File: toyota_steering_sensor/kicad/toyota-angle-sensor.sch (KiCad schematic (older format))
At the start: 30 parts, among them J1 AVR-ISP-6, J2 RJ45, U3 LS7366R, U5 AS5047P, U6 TJA1050, Y1 16MHz

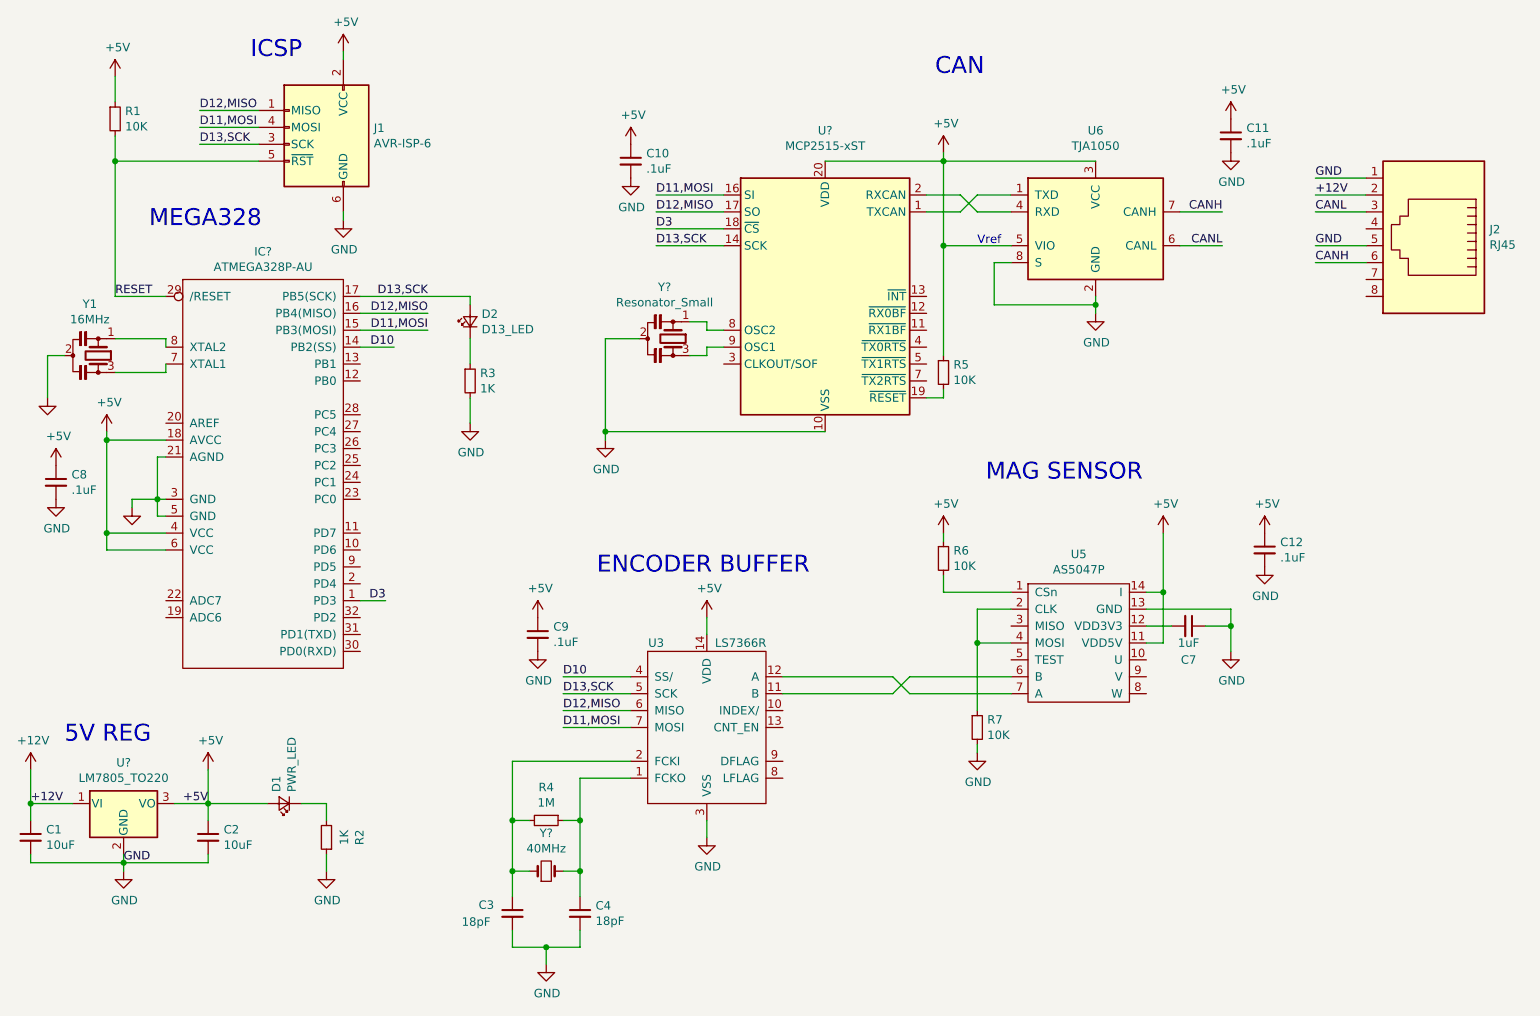
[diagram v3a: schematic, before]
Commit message: modified sch according to V2Changes.txt
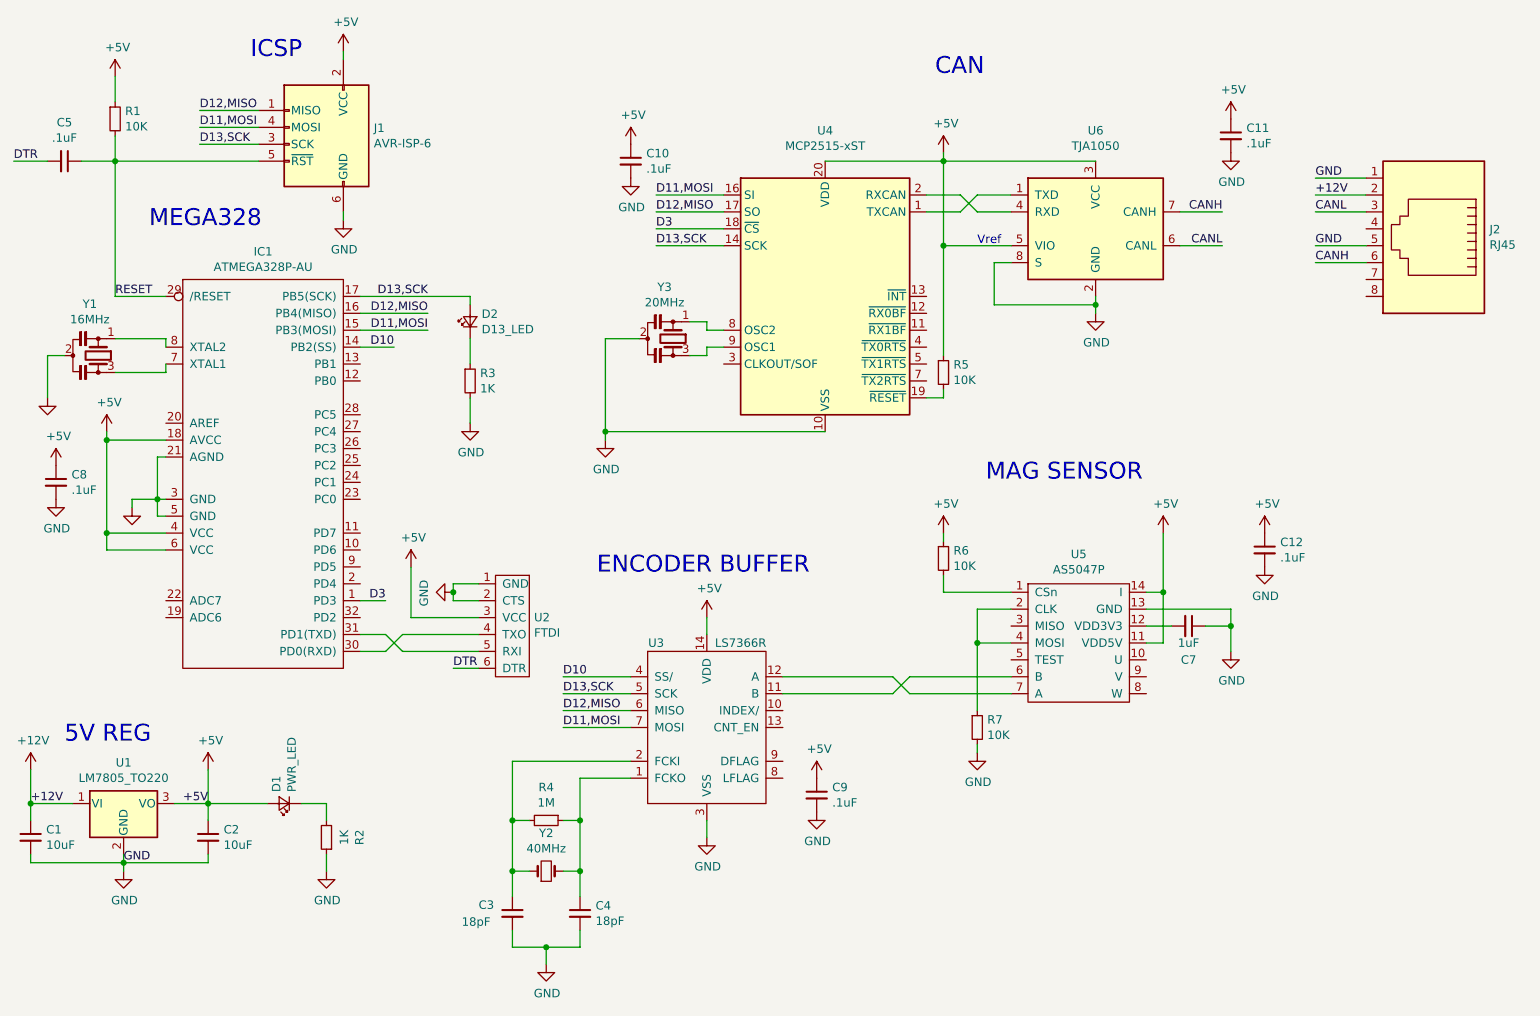
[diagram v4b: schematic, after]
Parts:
- added C5: .1uF, Capacitor_SMD:C_0603_1608Metric, symbol Device:C_Small
- added U2: FTDI, Connector_PinHeader_2.54mm:PinHeader_1x06_P2.54mm_Vertical_SMD_Pin1Left, symbol Angle_Sensor:FTDI
- IC1: renamed from IC?; footprint (none) -> Package_QFP:TQFP-32_7x7mm_P0.8mm
- Y1: footprint Crystal:Resonator_SMD_muRata_CSTxExxV-3Pin_3.0x1.1mm_HandSoldering -> Crystal:Resonator_SMD_muRata_CSTxExxV-3Pin_3.0x1.1mm
- Y3: renamed from Y?; value Resonator_Small -> 20MHz; footprint (none) -> Crystal:Resonator_SMD_muRata_CSTxExxV-3Pin_3.0x1.1mm
- gave numbers to parts that had none: 3
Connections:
- net +5V: now also U2.3 (VCC)
- net GND: now also U2.1 (GND), U2.2 (CTS)
- net RESET: now also C5.1
- net at IC1.30 (PD0(RXD)): now also U2.4 (TXO)
- net at IC1.31 (PD1(TXD)): now also U2.5 (RXI)
- new net DTR: C5.2, U2.6 (DTR)
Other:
- moved on the sheet: C9
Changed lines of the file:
@@
 F 0 "Y1" V 1095 2450 50  0000 C CNN
 F 1 "16MHz" V 1186 2450 50  0000 C CNN
-F 2 "Crystal:Resonator_SMD_muRata_CSTxExxV-3Pin_3.0x1.1mm_HandSoldering" H 1375 2500 50  0001 C CNN
+F 2 "Crystal:Resonator_SMD_muRata_CSTxExxV-3Pin_3.0x1.1mm" H 1375 2500 50  0001 C CNN
 F 3 "~" H 1375 2500 50  0001 C CNN
 F 4 "490-17948-1-ND" H 1400 2500 50  0001 C CNN "Digi-Key Part Number"
@@
 L power:+5V #PWR0103
 U 1 1 5D56B9CD
-P 4000 4050
-F 0 "#PWR0103" H 4000 3900 50  0001 C CNN
-F 1 "+5V" H 4015 4223 50  0000 C CNN
-F 2 "" H 4000 4050 50  0001 C CNN
-F 3 "" H 4000 4050 50  0001 C CNN
-	1    4000 4050
+P 5650 5000
+F 0 "#PWR0103" H 5650 4850 50  0001 C CNN
+F 1 "+5V" H 5665 5173 50  0000 C CNN
+F 2 "" H 5650 5000 50  0001 C CNN
+F 3 "" H 5650 5000 50  0001 C CNN
+	1    5650 5000
 	1    0    0    -1
 $EndComp
@@
 L power:GND #PWR0104
 U 1 1 5D56B9D3
-P 4000 4250
-F 0 "#PWR0104" H 4000 4000 50  0001 C CNN
-F 1 "GND" H 4005 4077 50  0000 C CNN
-F 2 "" H 4000 4250 50  0001 C CNN
-F 3 "" H 4000 4250 50  0001 C CNN
-	1    4000 4250
+P 5650 5200
+F 0 "#PWR0104" H 5650 4950 50  0001 C CNN
+F 1 "GND" H 5655 5027 50  0000 C CNN
+F 2 "" H 5650 5200 50  0001 C CNN
+F 3 "" H 5650 5200 50  0001 C CNN
+	1    5650 5200
 	1    0    0    -1
 $EndComp
@@
 L Device:C_Small C9
 U 1 1 5D56B9D9
-P 4000 4150
-F 0 "C9" H 4092 4196 50  0000 L CNN
-F 1 ".1uF" H 4092 4105 50  0000 L CNN
-F 2 "Capacitor_SMD:C_0603_1608Metric" H 4000 4150 50  0001 C CNN
-F 3 "~" H 4000 4150 50  0001 C CNN
-F 4 "1276-1000-1-ND" H 4000 4150 50  0001 C CNN "Digi-Key Part Number"
-	1    4000 4150
+P 5650 5100
+F 0 "C9" H 5742 5146 50  0000 L CNN
+F 1 ".1uF" H 5742 5055 50  0000 L CNN
+F 2 "Capacitor_SMD:C_0603_1608Metric" H 5650 5100 50  0001 C CNN
+F 3 "~" H 5650 5100 50  0001 C CNN
+F 4 "1276-1000-1-ND" H 5650 5100 50  0001 C CNN "Digi-Key Part Number"
+	1    5650 5100
 	1    0    0    -1
 $EndComp
@@
 $EndComp
 $Comp
-L Interface_CAN_LIN:MCP2515-xST U?
+L Interface_CAN_LIN:MCP2515-xST U4
 U 1 1 5D717111
 P 5700 2150
-F 0 "U?" H 5700 3131 50  0000 C CNN
+F 0 "U4" H 5700 3131 50  0000 C CNN
 F 1 "MCP2515-xST" H 5700 3040 50  0000 C CNN
 F 2 "Package_SO:TSSOP-20_4.4x6.5mm_P0.65mm" H 5700 1250 50  0001 C CIN
@@
 	1    0    0    -1
 $EndComp
-$Comp
-L Device:Resonator_Small Y?
-U 1 1 5D72675F
-P 4800 2400
-F 0 "Y?" V 4495 2350 50  0000 C CNN
-F 1 "Resonator_Small" V 4586 2350 50  0000 C CNN
-F 2 "" H 4775 2400 50  0001 C CNN
-F 3 "~" H 4775 2400 50  0001 C CNN
-	1    4800 2400
-	0    1    1    0
-$EndComp
 Wire Wire Line
 	5100 2350 5000 2350
@@
 	3850 5250 3850 5550
 $Comp
-L Device:Crystal_Small Y?
+L Device:Crystal_Small Y2
 U 1 1 5D73B9B9
 P 4050 5550
-F 0 "Y?" H 4050 5775 50  0000 C CNN
+F 0 "Y2" H 4050 5775 50  0000 C CNN
 F 1 "40MHz" H 4050 5684 50  0000 C CNN
 F 2 "Crystal:Crystal_SMD_Abracon_ABM3-2Pin_5.0x3.2mm" H 4050 5550 50  0001 C CNN
@@
 	3850 5550 3850 5700
 $Comp
-L Angle_Sensor:ATMEGA328P-AU IC?
+L Angle_Sensor:ATMEGA328P-AU IC1
 U 1 1 5D74BDEC
 P 2400 1950
-F 0 "IC?" H 2375 2015 50  0000 C CNN
+F 0 "IC1" H 2375 2015 50  0000 C CNN
 F 1 "ATMEGA328P-AU" H 2375 1924 50  0000 C CNN
-F 2 "" H 2400 -500 50  0001 C CNN
+F 2 "Package_QFP:TQFP-32_7x7mm_P0.8mm" H 2400 -500 50  0001 C CNN
 F 3 "" H 2400 -500 50  0001 C CNN
 	1    2400 1950
@@
 $EndComp
 $Comp
-L Regulator_Linear:LM7805_TO220 U?
+L Regulator_Linear:LM7805_TO220 U1
 U 1 1 5D74D832
 P 1550 5150
-F 0 "U?" H 1550 5392 50  0000 C CNN
+F 0 "U1" H 1550 5392 50  0000 C CNN
 F 1 "LM7805_TO220" H 1550 5301 50  0000 C CNN
 F 2 "Package_TO_SOT_THT:TO-220-3_Vertical" H 1550 5375 50  0001 C CIN
@@
 	1    0    0    -1
 $EndComp
+$Comp
+L Device:Resonator_Small Y3
+U 1 1 5D72675F
+P 4800 2400
+F 0 "Y3" V 4495 2350 50  0000 C CNN
+F 1 "20MHz" V 4586 2350 50  0000 C CNN
+F 2 "Crystal:Resonator_SMD_muRata_CSTxExxV-3Pin_3.0x1.1mm" H 4775 2400 50  0001 C CNN
+F 3 "~" H 4775 2400 50  0001 C CNN
+	1    4800 2400
+	0    1    1    0
+$EndComp
+$Comp
+L Angle_Sensor:FTDI U2
+U 1 1 5D759EA1
+P 3850 3750
+F 0 "U2" H 3722 3451 50  0000 R CNN
+F 1 "FTDI" H 3722 3360 50  0000 R CNN
+F 2 "Connector_PinHeader_2.54mm:PinHeader_1x06_P2.54mm_Vertical_SMD_Pin1Left" H 3850 3750 50  0001 C CNN
+F 3 "" H 3850 3750 50  0001 C CNN
+	1    3850 3750
+	-1   0    0    -1
+$EndComp
+Wire Wire Line
+	3200 4250 3100 4150
+Wire Wire Line
+	3100 4150 2950 4150
+Wire Wire Line
+	3200 4150 3100 4250
+Wire Wire Line
+	3100 4250 2950 4250
+Wire Wire Line
+	3200 4150 3650 4150
+Wire Wire Line
+	3200 4250 3650 4250
+$Comp
+L power:GND #PWR0113
+U 1 1 5D7A8FBA
+P 3500 3900
+F 0 "#PWR0113" H 3500 3650 50  0001 C CNN
+F 1 "GND" H 3505 3727 50  0000 C CNN
+F 2 "" H 3500 3900 50  0001 C CNN
+F 3 "" H 3500 3900 50  0001 C CNN
+	1    3500 3900
+	0    1    1    0
+$EndComp
+$Comp
+L power:+5V #PWR0114
+U 1 1 5D7A21D2
+P 3250 3750
+F 0 "#PWR0114" H 3250 3600 50  0001 C CNN
+F 1 "+5V" H 3265 3923 50  0000 C CNN
+F 2 "" H 3250 3750 50  0001 C CNN
+F 3 "" H 3250 3750 50  0001 C CNN
+	1    3250 3750
+	1    0    0    -1
+$EndComp
+Wire Wire Line
+	3650 4050 3250 4050
+Wire Wire Line
+	3250 4050 3250 3750
+Wire Wire Line
+	3650 3950 3500 3950
+Wire Wire Line
+	3500 3950 3500 3900
+Wire Wire Line
+	3650 3850 3500 3850
+Wire Wire Line
+	3500 3850 3500 3900
+Connection ~ 3500 3900
+Wire Wire Line
+	3650 4350 3500 4350
+Text Label 3500 4350 0    50   ~ 0
+DTR
+$Comp
+L Device:C_Small C5
+U 1 1 5D7E7EAD
+P 1200 1350
+F 0 "C5" V 971 1350 50  0000 C CNN
+F 1 ".1uF" V 1062 1350 50  0000 C CNN
+F 2 "Capacitor_SMD:C_0603_1608Metric" H 1200 1350 50  0001 C CNN
+F 3 "~" H 1200 1350 50  0001 C CNN
+	1    1200 1350
+	0    1    1    0
+$EndComp
+Wire Wire Line
+	1300 1350 1500 1350
+Wire Wire Line
+	1100 1350 900  1350
+Text Label 900  1350 0    50   ~ 0
+DTR
 $EndSCHEMATC

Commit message: done routing v2
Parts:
- U2: footprint Connector_PinHeader_2.54mm:PinHeader_1x06_P2.54mm_Vertical_SMD_Pin1Left -> Connector_PinHeader_1.27mm:PinHeader_1x06_P1.27mm_Vertical_SMD_Pin1Left
- U3: footprint Package_SO:SOIC-14_3.9x8.7mm_P1.27mm -> Package_SO:TSSOP-14_4.4x5mm_P0.65mm
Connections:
- net D13,SCK: now also R3.1; no longer D2.2 (A)
- net GND: now also D2.1 (K); no longer R3.2
- new net: D2.2 (A), R3.2
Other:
- moved on the sheet: D2, R3
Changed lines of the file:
@@
 	7950 4100 8100 4100
-$Comp
-L Device:LED_Small D2
-U 1 1 5D506383
-P 3600 2300
-F 0 "D2" V 3646 2232 50  0000 R CNN
-F 1 "D13_LED" V 3555 2232 50  0000 R CNN
-F 2 "LED_SMD:LED_0805_2012Metric" V 3600 2300 50  0001 C CNN
-F 3 "~" V 3600 2300 50  0001 C CNN
-F 4 "475-1410-1-ND" H 3600 2300 50  0001 C CNN "Digi-Key Part Number"
-	1    3600 2300
-	0    -1   -1   0
-$EndComp
 $Comp
 L Device:R_Small R3
 U 1 1 5D509B73
-P 3600 2650
-F 0 "R3" H 3659 2696 50  0000 L CNN
-F 1 "1K" H 3659 2605 50  0000 L CNN
-F 2 "Resistor_SMD:R_0603_1608Metric" H 3600 2650 50  0001 C CNN
-F 3 "~" H 3600 2650 50  0001 C CNN
-F 4 "A130091CT-ND " H 3600 2650 50  0001 C CNN "Digi-Key Part Number"
-	1    3600 2650
+P 3600 2300
+F 0 "R3" H 3659 2346 50  0000 L CNN
+F 1 "1K" H 3659 2255 50  0000 L CNN
+F 2 "Resistor_SMD:R_0603_1608Metric" H 3600 2300 50  0001 C CNN
+F 3 "~" H 3600 2300 50  0001 C CNN
+F 4 "A130091CT-ND " H 3600 2300 50  0001 C CNN "Digi-Key Part Number"
+	1    3600 2300
 	1    0    0    -1
 $EndComp
@@
 F 0 "U3" H 4700 4300 50  0000 C CNN
 F 1 "LS7366R" H 5200 4300 50  0000 C CNN
-F 2 "Package_SO:SOIC-14_3.9x8.7mm_P1.27mm" H 4700 4300 50  0001 C CNN
+F 2 "Package_SO:TSSOP-14_4.4x5mm_P0.65mm" H 4700 4300 50  0001 C CNN
 F 3 "" H 4700 4300 50  0001 C CNN
 F 4 "N/A" H 5000 4250 50  0001 C CNN "Digi-Key Part Number"
@@
 F 0 "U2" H 3722 3451 50  0000 R CNN
 F 1 "FTDI" H 3722 3360 50  0000 R CNN
-F 2 "Connector_PinHeader_2.54mm:PinHeader_1x06_P2.54mm_Vertical_SMD_Pin1Left" H 3850 3750 50  0001 C CNN
+F 2 "Connector_PinHeader_1.27mm:PinHeader_1x06_P1.27mm_Vertical_SMD_Pin1Left" H 3850 3750 50  0001 C CNN
 F 3 "" H 3850 3750 50  0001 C CNN
 	1    3850 3750
@@
 Text Label 900  1350 0    50   ~ 0
 DTR
+$Comp
+L Device:LED_Small D2
+U 1 1 5D506383
+P 3600 2650
+F 0 "D2" V 3646 2582 50  0000 R CNN
+F 1 "D13_LED" V 3555 2582 50  0000 R CNN
+F 2 "LED_SMD:LED_0805_2012Metric" V 3600 2650 50  0001 C CNN
+F 3 "~" V 3600 2650 50  0001 C CNN
+F 4 "475-1410-1-ND" H 3600 2650 50  0001 C CNN "Digi-Key Part Number"
+	1    3600 2650
+	0    -1   -1   0
+$EndComp
 $EndSCHEMATC

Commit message: updated BOM for V2
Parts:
- C5: Digi-Key Part Number (none) -> 1276-1000-1-ND
- IC1: Digi-Key Part Number (none) -> ATMEGA328P-AU-ND
- J2: Digi-Key Part Number 609-1046-ND -> WM3547CT-ND
- U1: Digi-Key Part Number (none) -> 296-47192-ND
- U2: Digi-Key Part Number (none) -> N/A
- U4: Digi-Key Part Number (none) -> MCP2515T-I/ST
- Y2: Digi-Key Part Number (none) -> 535-9114-1-ND
- Y3: Digi-Key Part Number (none) -> 490-17957-1-ND
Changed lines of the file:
@@
 F 2 "ZSS:Molex 855025008 RJ45" V 9300 1775 50  0001 C CNN
 F 3 "~" V 9300 1775 50  0001 C CNN
-F 4 "609-1046-ND" H 9300 1750 50  0001 C CNN "Digi-Key Part Number"
+F 4 "WM3547CT-ND" H 9300 1750 50  0001 C CNN "Digi-Key Part Number"
 	1    9300 1750
 	-1   0    0    1
@@
 F 2 "Package_SO:TSSOP-20_4.4x6.5mm_P0.65mm" H 5700 1250 50  0001 C CIN
 F 3 "http://ww1.microchip.com/downloads/en/DeviceDoc/21801e.pdf" H 5800 1350 50  0001 C CNN
+F 4 "MCP2515T-I/ST" H 0   0   50  0001 C CNN "Digi-Key Part Number"
 	1    5700 2150
 	1    0    0    -1
@@
 F 2 "Crystal:Crystal_SMD_Abracon_ABM3-2Pin_5.0x3.2mm" H 4050 5550 50  0001 C CNN
 F 3 "~" H 4050 5550 50  0001 C CNN
+F 4 "535-9114-1-ND" H 0   0   50  0001 C CNN "Digi-Key Part Number"
 	1    4050 5550
 	1    0    0    -1
@@
 F 2 "Package_QFP:TQFP-32_7x7mm_P0.8mm" H 2400 -500 50  0001 C CNN
 F 3 "" H 2400 -500 50  0001 C CNN
+F 4 "ATMEGA328P-AU-ND" H 0   0   50  0001 C CNN "Digi-Key Part Number"
 	1    2400 1950
 	1    0    0    -1
@@
 F 2 "Package_TO_SOT_THT:TO-220-3_Vertical" H 1550 5375 50  0001 C CIN
 F 3 "http://www.fairchildsemi.com/ds/LM/LM7805.pdf" H 1550 5100 50  0001 C CNN
+F 4 "296-47192-ND" H 0   0   50  0001 C CNN "Digi-Key Part Number"
 	1    1550 5150
 	1    0    0    -1
@@
 F 2 "Crystal:Resonator_SMD_muRata_CSTxExxV-3Pin_3.0x1.1mm" H 4775 2400 50  0001 C CNN
 F 3 "~" H 4775 2400 50  0001 C CNN
+F 4 "490-17957-1-ND" H 0   0   50  0001 C CNN "Digi-Key Part Number"
 	1    4800 2400
 	0    1    1    0
@@
 F 2 "Connector_PinHeader_1.27mm:PinHeader_1x06_P1.27mm_Vertical_SMD_Pin1Left" H 3850 3750 50  0001 C CNN
 F 3 "" H 3850 3750 50  0001 C CNN
+F 4 "N/A" H 0   0   50  0001 C CNN "Digi-Key Part Number"
 	1    3850 3750
 	-1   0    0    -1
@@
 F 2 "Capacitor_SMD:C_0603_1608Metric" H 1200 1350 50  0001 C CNN
 F 3 "~" H 1200 1350 50  0001 C CNN
+F 4 "1276-1000-1-ND" H 0   0   50  0001 C CNN "Digi-Key Part Number"
 	1    1200 1350
 	0    1    1    0
